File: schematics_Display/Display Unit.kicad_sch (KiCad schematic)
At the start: 8 parts, among them M1 Stepper_Motor_bipolar, U2 XIAO_ESP32C3, U3 Press Buttom

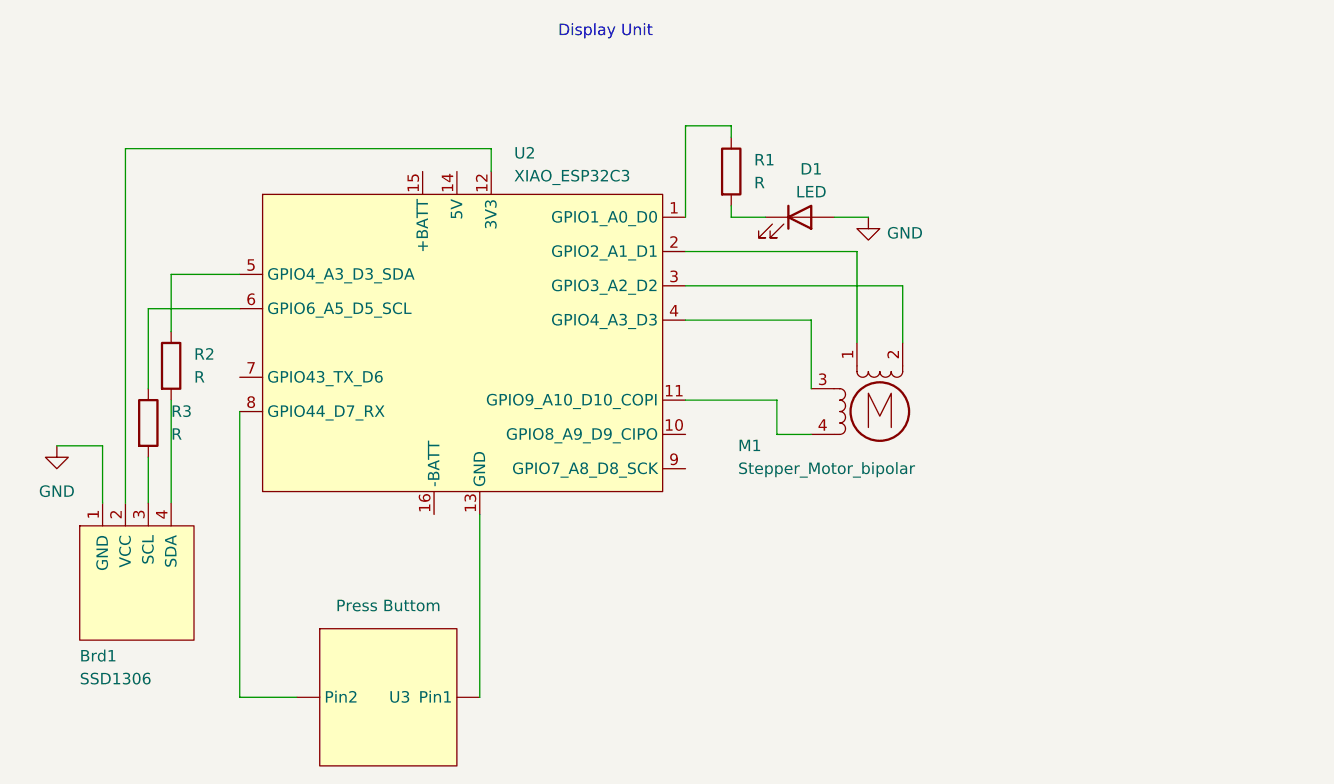
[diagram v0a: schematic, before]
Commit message: Add sensor unit test coed
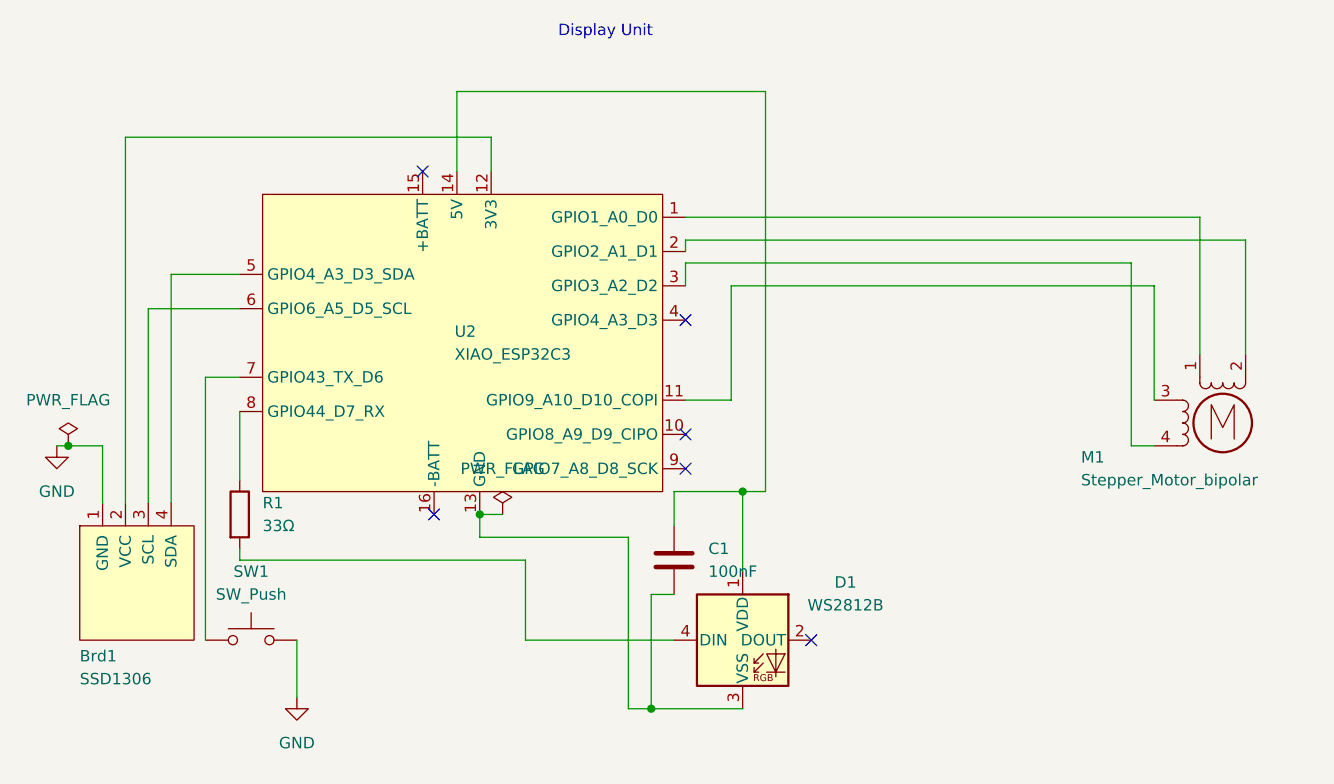
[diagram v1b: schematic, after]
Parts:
- removed D1: LED, symbol Device:LED
- removed R2, R3: R, symbol Device:R
- removed U3: Press Buttom, symbol my library:Push_Button
- added C1: 100nF, Capacitor_SMD:C_0805_2012Metric, symbol Device:C
- added D1: WS2812B, LED_SMD:LED_WS2812B_PLCC4_5.0x5.0mm_P3.2mm, symbol LED:WS2812B
- added SW1: SW_Push, Button_Switch_THT:SW_PUSH_6mm_H4.3mm, symbol Switch:SW_Push
- Brd1: footprint (none) -> Display:128x64OLED
- M1: footprint (none) -> Motors:x27_stepper_two_holes
- R1: value R -> 33Ω; footprint (none) -> Resistor_SMD:R_0805_2012Metric
- U2: footprint (none) -> RF_Module:XIAO_ESP32
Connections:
- net GND: now also SW1.2
- net at R1.2: now also D1.4 (DIN)
- net at U2.13 (GND): now also C1.2, D1.3 (VSS)
- net at U2.8 (GPIO44_D7_RX): now also R1.1
- net at Brd1.3 (SCL): now also U2.6 (GPIO6_A5_D5_SCL)
- net at Brd1.4 (SDA): now also U2.5 (GPIO4_A3_D3_SDA)
- net at M1.1: now also U2.1 (GPIO1_A0_D0); no longer U2.2 (GPIO2_A1_D1)
- net at M1.2 (-): now also U2.2 (GPIO2_A1_D1); no longer U2.3 (GPIO3_A2_D2)
- net at M1.3: now also U2.11 (GPIO9_A10_D10_COPI); no longer U2.4 (GPIO4_A3_D3)
- net at M1.4: now also U2.3 (GPIO3_A2_D2); no longer U2.11 (GPIO9_A10_D10_COPI)
- net at U2.14 (5V): now also C1.1, D1.1 (VDD)
- net at U2.7 (GPIO43_TX_D6): now also SW1.1
- no-connect marks 0 -> 6
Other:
- moved on the sheet: M1

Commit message: add coding, pcb, and revised sketches
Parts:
- C1: footprint Capacitor_SMD:C_0805_2012Metric -> Capacitor_SMD:C_0805_2012Metric_Pad1.18x1.45mm_HandSolder
- R1: footprint Resistor_SMD:R_0805_2012Metric -> Resistor_SMD:R_0805_2012Metric_Pad1.20x1.40mm_HandSolder
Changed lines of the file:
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@@
 			)
 		)
-		(property "Footprint" "Resistor_SMD:R_0805_2012Metric"
+		(property "Footprint" "Resistor_SMD:R_0805_2012Metric_Pad1.20x1.40mm_HandSolder"
 			(at 125.222 102.87 90)
 			(effects
@@
 			)
 		)
-		(property "Footprint" "Capacitor_SMD:C_0805_2012Metric"
+		(property "Footprint" "Capacitor_SMD:C_0805_2012Metric_Pad1.18x1.45mm_HandSolder"
 			(at 176.2252 111.76 0)
 			(effects
